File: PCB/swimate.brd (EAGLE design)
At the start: 100 x 80 mm, 54 parts, among them IC1 LPC11U24, T1 BSS84, T2 BSS84, U1 USD-SOCKETNEW, U5 DS3231MZ/V+T, U6 MAX1595EUA33+, U7 MAX1811ESA-T, U8 MAX16054AZT+T, U9 HC_05, Y1 12.000MHz

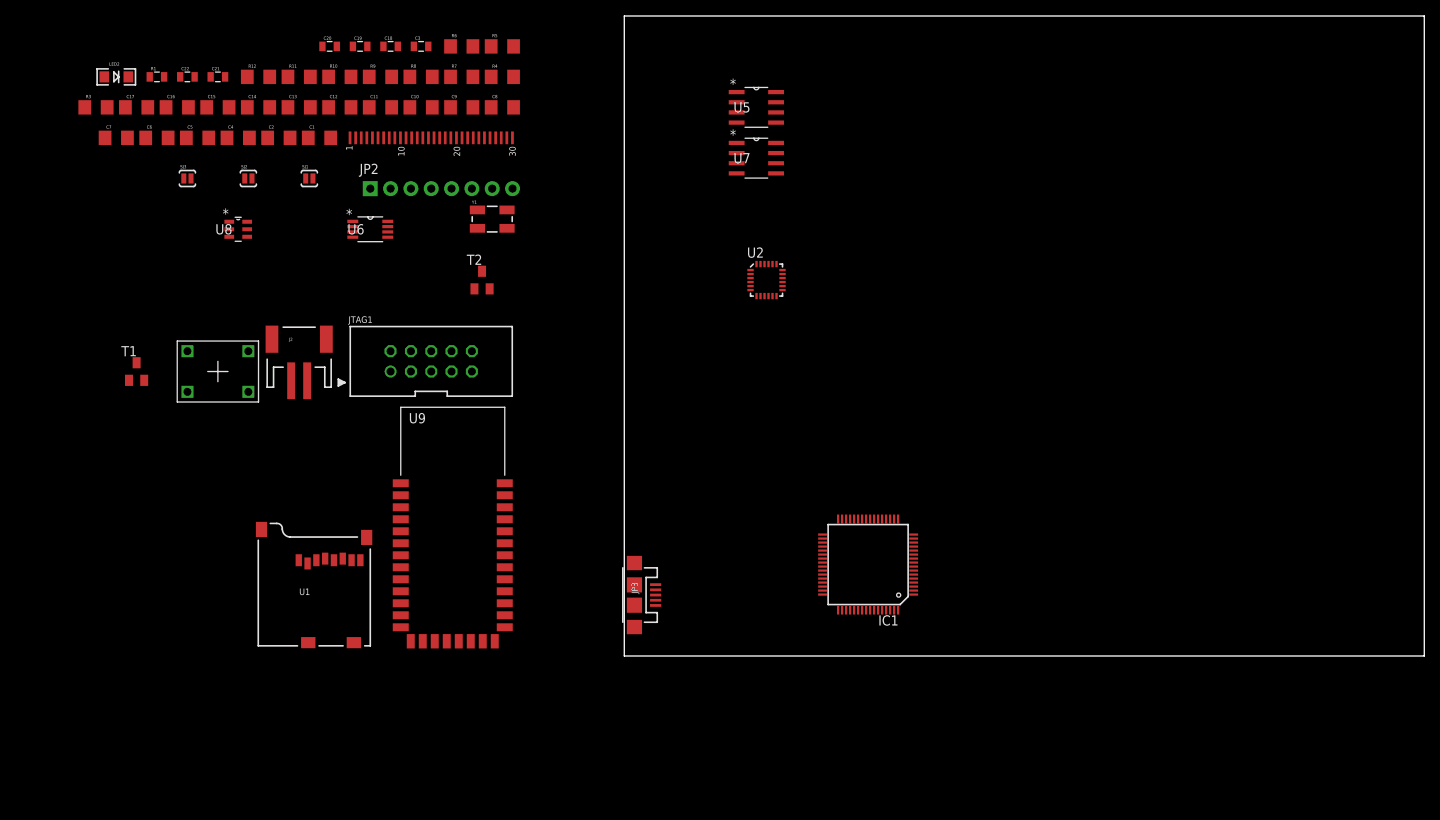
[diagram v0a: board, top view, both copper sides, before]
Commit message: Starting Board layout.. still some pins to route
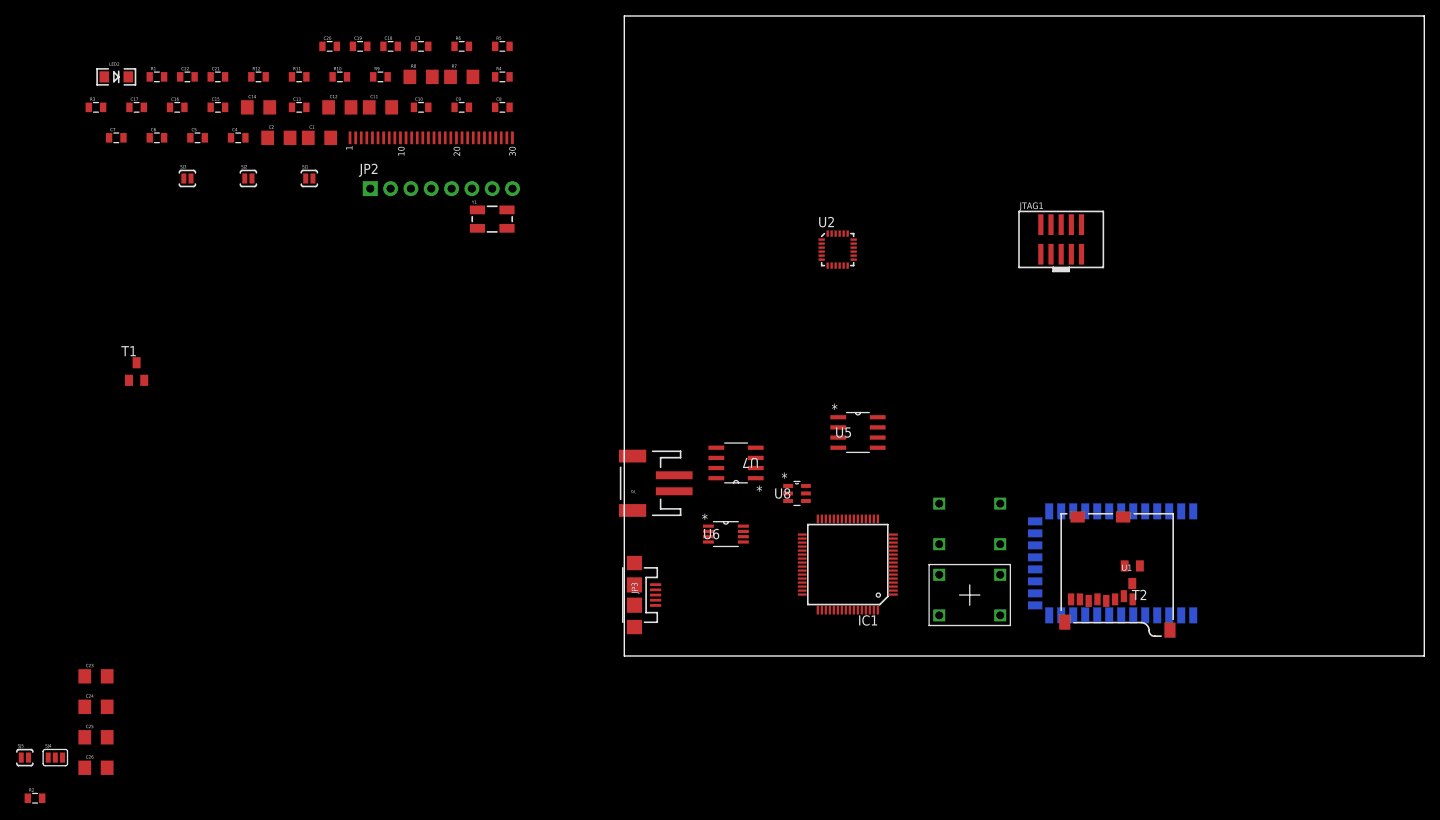
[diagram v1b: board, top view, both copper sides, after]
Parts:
- added C23, C24: 10uF, SparkFun-Capacitors:1206
- added C25, C26: 100nF, SparkFun-Capacitors:1206
- added R2: 2k, SparkFun-Passives:0805
- added SJ4: (no value), SparkFun-Passives:SJ_3
- added SJ5: SOLDERJUMPERNO, SparkFun-Passives:SJ_2S-NO
- added SW_MODE: (no value), SparkFun-Electromechanical:KSA_SEALED_TAC_SWITCH
- C10, C13, C15, C16, C17, C4, C5, C6, C7, C8, C9: device SparkFun-Capacitors:1206 -> SparkFun-Passives:0805
- JTAG1: device microbuilder:CORTEXM3_SWD10_MOLEX -> microbuilder:2X05_1.27MM_SMT
- R10, R11, R12, R3, R4: device SparkFun-Passives:1206 -> SparkFun-Passives:0805
- R5, R6: value (none) -> 10k; device SparkFun-Passives:1206 -> SparkFun-Passives:0805
- R8: value 10k -> 24k
- R9: value 10k -> 24K; device SparkFun-Passives:1206 -> SparkFun-Passives:0805
- moved SW_PWR 95.9 mm to (43.2, 16.5), flipped to the bottom
- moved T2 89.2 mm to (63.5, 10.2), turned to 180 degrees
- moved U9 89.1 mm to (67.3, 11.4), flipped to the bottom, turned to 90 degrees
- moved U1 87.9 mm to (54.6, 17.8), turned to 180 degrees
- moved JTAG1 80.2 mm to (54.6, 52.1)
- moved U8 77.3 mm to (21.6, 20.3)
- moved U6 58.5 mm to (12.7, 15.2)
- moved J2 46.2 mm to (2.54, 21.6), turned to 90 degrees
- moved U5 42.6 mm to (29.2, 27.9)
- moved U7 38.2 mm to (14.0, 24.1), turned to 180 degrees
- moved U2 9.67 mm to (26.7, 50.8)
- moved IC1 2.54 mm to (27.9, 11.4)
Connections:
- net N$6 renamed SPI1_MISO
- removed net N$22: IC1.18
- removed net PIO_0: JTAG1.10
- removed net PIO_10: JTAG1.4, R4.2
- removed net PIO_15: JTAG1.2, R3.1
- removed net PIO_9: JTAG1.6
- new net BOOTLOAD: IC1.5, SJ5.2
- new net N$6: C23.1, C24.1, C25.1, C26.1, IC1.10, IC1.33, IC1.48, IC1.58
- new net SPI_MISO0: IC1.36
- new net SPI_MOSI0: IC1.37, JTAG1.6
- new net SWCLK: IC1.38, JTAG1.4, R4.2
- new net SWDIO: IC1.52, JTAG1.2, R3.1
- new net SW_MODE: SW_MODE.P$3, SW_MODE.P$4
- new net VDISPLAY: C19.2, SJ4.2, U$1.6
- net 3.3V: now also SJ4.1
- net BT_ENABLE: no longer SJ3.2
- net GND: now also C16.1, C17.1, C23.2, C24.2, C25.2, C26.2, IC1.54, IC1.7, R2.1, SW_MODE.P$1, SW_MODE.P$2, SW_PWR.P$1; no longer C16.2, C17.2
- net I2C_SCL: now also IC1.20
- net I2C_SDA: now also IC1.21
- net N$1: now also SW_PWR.P$3
- net N$15: now also SJ3.2
- net N$17: now also C17.2; no longer C17.1
- net N$18: now also C16.2; no longer C16.1
- net N$21: now also R2.2, SJ5.1; no longer IC1.51
- net RST: now also IC1.4, JTAG1.10
- net SPI1_MOSI: now also IC1.51
- net SPI1_SCK: now also IC1.18
- net USB_SCON: now also IC1.29
- net VBAT: now also SJ4.3; no longer C19.2, U$1.6
- net VUSB: now also IC1.19

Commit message: More work on layout
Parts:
- C1, C2: device SparkFun-Capacitors:1206 -> SparkFun-Passives:0805
- C23, C24, C25, C26: device SparkFun-Capacitors:1206 -> SparkFun-Capacitors:0805
- R7, R8: device SparkFun-Passives:1206 -> SparkFun-Passives:0805
- moved SJ4 163.3 mm to (86.4, 30.5)
- moved C21 154.4 mm to (97.8, 30.5), turned to 180 degrees
- moved C22 154.0 mm to (94.0, 31.8)
- moved R1 153.7 mm to (90.2, 33.0)
- moved R3 150.3 mm to (74.9, 16.5)
- moved C7 137.4 mm to (73.7, 57.1)
- moved C20 135.4 mm to (90.2, 29.2)
- moved C5 133.4 mm to (80.0, 63.5)
- moved C6 132.1 mm to (73.7, 61.0)
- moved C19 127.6 mm to (85.1, 27.9)
- moved C4 123.2 mm to (74.9, 63.5)
- moved C18 120.8 mm to (82.5, 30.5), turned to 180 degrees
- moved U$1 119.7 mm to (88.9, 25.4)
- moved JP2 118.3 mm to (86.4, 52.1), turned to 90 degrees
- moved C3 113.7 mm to (78.7, 30.5), turned to 180 degrees
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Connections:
- removed net N$10: U9.11
- net RST: now also U9.11
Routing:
- net GND: track 0.00 -> 47.9 mm
- net VUSB: track 0.00 -> 24.2 mm, vias 0 -> 1
- net N$1: track 0.00 -> 22.1 mm
- net N$12: track 0.00 -> 11.5 mm
- net VBAT: track 0.00 -> 6.25 mm
- net N$17: track 0.00 -> 5.12 mm
- net N$20: track 0.00 -> 4.50 mm
- net CHARGE_STAT: track 0.00 -> 4.14 mm
- net N$19: track 0.00 -> 3.88 mm
- net N$14: track 0.00 -> 3.47 mm
- net N$13: track 0.00 -> 3.47 mm
- net N$16: track 0.00 -> 2.98 mm
- net SYS_SHUTDOWN: track 0.00 -> 2.73 mm
- net N$8: track 0.00 -> 2.68 mm
- net N$18: track 0.00 -> 2.01 mm
